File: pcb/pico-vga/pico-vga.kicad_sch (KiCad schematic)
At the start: 32 parts, among them J1 DB15_Female_HighDensity, J2 Micro_SD_Card, J3 AudioJack3, J8 Conn_01x05_Male, J9 Conn_01x02_Male, SW1 SW_Push, U1 Raspberry_Pi_Pico, U2 74LVC2G34

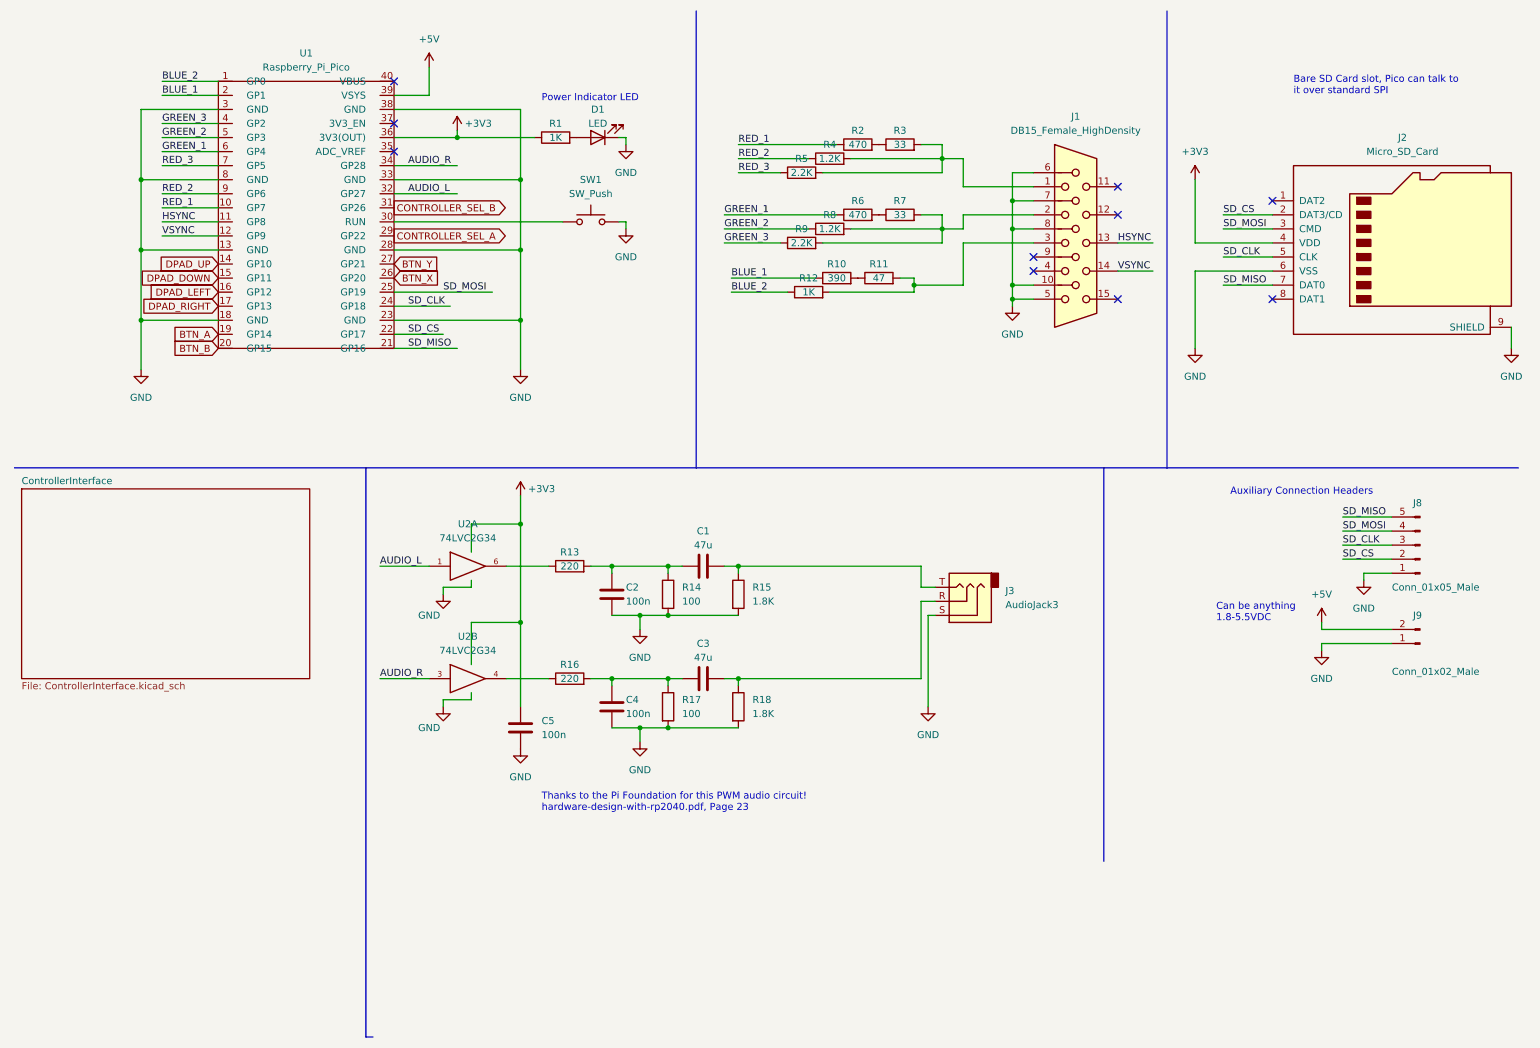
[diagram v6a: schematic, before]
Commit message: PCB v2 done
This update removed most of the stuff on the board -- the massive controller multiplexer is now replaced with an ATTiny24 on the controller side and an I2C bus. The buffer for the audio circuit is also gone. The board now supports surface mounting the pico, and is significantly smaller.
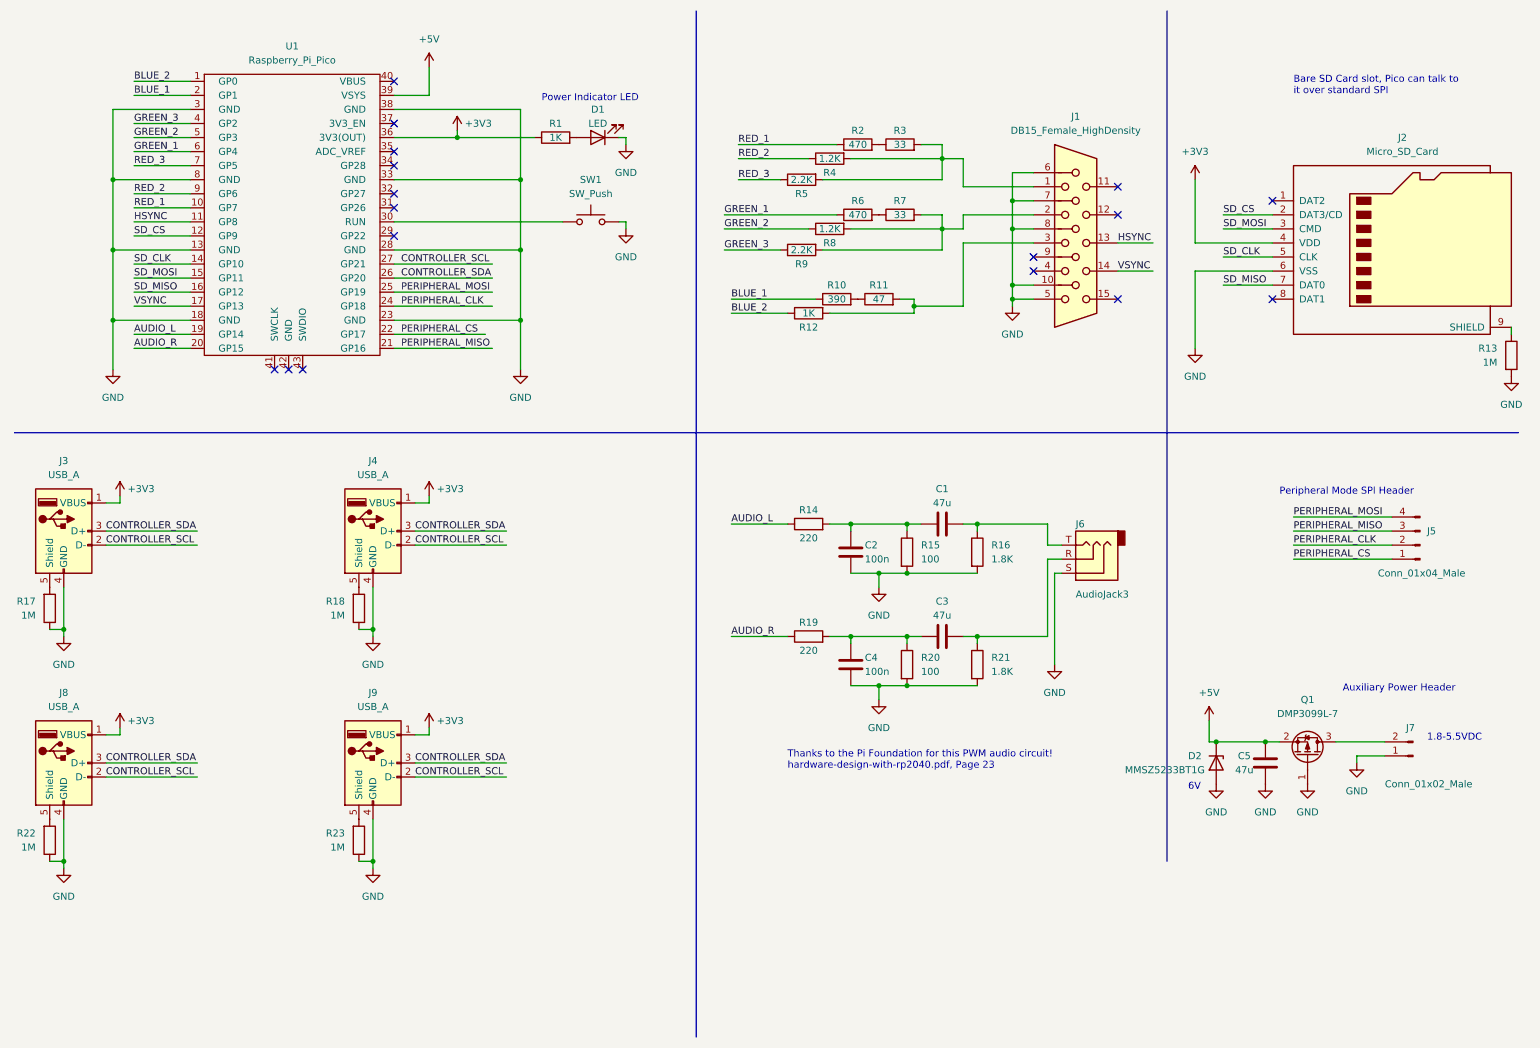
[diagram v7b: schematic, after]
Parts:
- removed J8: Conn_01x05_Male, Connector_PinHeader_2.54mm:PinHeader_1x05_P2.54mm_Horizontal, symbol Connector:Conn_01x05_Male
- removed U2: 74LVC2G34, Package_SO:TSOP-6_1.65x3.05mm_P0.95mm, symbol 74xGxx:74LVC2G34
- added D2: MMSZ5233BT1G, Diode_SMD:D_SOD-123, symbol Device:D_Zener
- added J3, J4, J8, J9: USB_A, Connector_USB:USB_A_Molex_67643_Horizontal, symbol Connector:USB_A
- added J5: Conn_01x04_Male, Connector_PinHeader_2.54mm:PinHeader_1x04_P2.54mm_Horizontal, symbol Connector:Conn_01x04_Male
- added Q1: DMP3099L-7, Package_TO_SOT_SMD:SOT-23, symbol Device:Q_PMOS_GSD
- added R13, R17, R18, R22, R23: 1M, Resistor_SMD:R_0805_2012Metric_Pad1.20x1.40mm_HandSolder, symbol Device:R
- C1, C2, C3, C4: footprint Capacitor_SMD:C_0603_1608Metric_Pad1.08x0.95mm_HandSolder -> Capacitor_SMD:C_0805_2012Metric_Pad1.18x1.45mm_HandSolder
- C5: value 100n -> 47u; footprint Capacitor_SMD:C_0603_1608Metric_Pad1.08x0.95mm_HandSolder -> Capacitor_SMD:C_0805_2012Metric_Pad1.18x1.45mm_HandSolder
- J1: Part Number (none) -> L77HDE15SD1CH4FVGA
- J2: Part Number (none) -> DM3AT-SF-PEJM5
- J6: renamed from J3; Part Number (none) -> SJ1-3533NG
- R1, R10, R11, R12, R2, R3, R4, R5, R6, R7, R8, R9: footprint Resistor_SMD:R_0603_1608Metric_Pad0.98x0.95mm_HandSolder -> Resistor_SMD:R_0805_2012Metric_Pad1.20x1.40mm_HandSolder
- R14: renamed from R13; footprint Resistor_SMD:R_0603_1608Metric_Pad0.98x0.95mm_HandSolder -> Resistor_SMD:R_0805_2012Metric_Pad1.20x1.40mm_HandSolder
- R15: renamed from R14; footprint Resistor_SMD:R_0603_1608Metric_Pad0.98x0.95mm_HandSolder -> Resistor_SMD:R_0805_2012Metric_Pad1.20x1.40mm_HandSolder
- R16: renamed from R15; footprint Resistor_SMD:R_0603_1608Metric_Pad0.98x0.95mm_HandSolder -> Resistor_SMD:R_0805_2012Metric_Pad1.20x1.40mm_HandSolder
- R19: renamed from R16; footprint Resistor_SMD:R_0603_1608Metric_Pad0.98x0.95mm_HandSolder -> Resistor_SMD:R_0805_2012Metric_Pad1.20x1.40mm_HandSolder
- R20: renamed from R17; footprint Resistor_SMD:R_0603_1608Metric_Pad0.98x0.95mm_HandSolder -> Resistor_SMD:R_0805_2012Metric_Pad1.20x1.40mm_HandSolder
- R21: renamed from R18; footprint Resistor_SMD:R_0603_1608Metric_Pad0.98x0.95mm_HandSolder -> Resistor_SMD:R_0805_2012Metric_Pad1.20x1.40mm_HandSolder
- renumbered J9 to J7
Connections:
- net BTN_A is gone; now on net AUDIO_L: U1.19 (GP14)
- net BTN_B is gone; now on net AUDIO_R: U1.20 (GP15)
- net DPAD_DOWN is gone; now on net SD_MOSI: U1.15 (GP11)
- net DPAD_LEFT is gone; now on net SD_MISO: U1.16 (GP12)
- net DPAD_RIGHT is gone; now on net VSYNC: U1.17 (GP13)
- net DPAD_UP is gone; now on net SD_CLK: U1.14 (GP10)
- net +3V3: now also J3.1 (VBUS), J4.1 (VBUS), J8.1 (VBUS), J9.1 (VBUS); no longer C5.1
- net +5V: now also C5.2, D2.1 (K), Q1.2 (S); no longer J7.2 (Pin_2)
- net AUDIO_L: now also R14.1; no longer U1.32 (GP27)
- net AUDIO_R: now also R19.1; no longer U1.34 (GP28)
- net GND: now also C5.1, D2.2 (A), J3.4 (GND), J4.4 (GND), J8.4 (GND), J9.4 (GND), Q1.1 (G), R13.2, R17.1, R18.1, R22.1, R23.1; no longer C5.2, J2.9 (SHIELD)
- net SD_CLK: no longer U1.24 (GP18)
- net SD_CS: now also U1.12 (GP9); no longer U1.22 (GP17)
- net SD_MISO: no longer U1.21 (GP16)
- net SD_MOSI: no longer U1.25 (GP19)
- net VSYNC: no longer U1.12 (GP9)
- net BTN_X renamed CONTROLLER_SDA
- net CONTROLLER_SDA: now also J3.3 (D+), J4.3 (D+), J8.3 (D+), J9.3 (D+)
- net BTN_Y renamed CONTROLLER_SCL
- net CONTROLLER_SCL: now also J3.2 (D-), J4.2 (D-), J8.2 (D-), J9.2 (D-)
- net CONTROLLER_SEL_A: no longer names the net of U1.29 (GP22)
- net CONTROLLER_SEL_B: no longer names the net of U1.31 (GP26)
- new net: J9.5 (Shield), R23.2
- new net: J4.5 (Shield), R18.2
- new net: J3.5 (Shield), R17.2
- new net: J2.9 (SHIELD), R13.1
- new net: J8.5 (Shield), R22.2
- new net: J7.2 (Pin_2), Q1.3 (D)
- new net PERIPHERAL_CLK: J5.2 (Pin_2), U1.24 (GP18)
- new net PERIPHERAL_CS: J5.1 (Pin_1), U1.22 (GP17)
- new net PERIPHERAL_MISO: J5.3 (Pin_3), U1.21 (GP16)
- new net PERIPHERAL_MOSI: J5.4 (Pin_4), U1.25 (GP19)
- no-connect marks 10 -> 17
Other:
- removed sheet ControllerInterface
- note added: "1.8-5.5VDC"
- note added: "6V"
- note added: "Auxiliary Power Header"
- note added: "Peripheral Mode SPI Header"
- note removed: "Auxiliary Connection Headers"
- note removed: "Can be anything 1.8-5.5VDC"
- moved on the sheet: C1, C2, C3, C4, J6, J7, R10, R11, R12, R14, R15, R16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

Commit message: PCB update and BOM
Remade the BOM so now you can just export to csv and throw it into digikey, makes it a lot easier. In making the BOM I realized some of my old parts were super expensive, so I redid some components
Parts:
- removed J2: Micro_SD_Card, Connector_Card:microSD_HC_Hirose_DM3AT-SF-PEJM5, symbol Connector:Micro_SD_Card
- added J2: Micro_SD_Card_Det, pico-vga:MEM2061-01-188-00-A_GCT, symbol Connector:Micro_SD_Card_Det
- J6: footprint Connector_Audio:Jack_3.5mm_CUI_SJ1-3533NG_Horizontal -> pico-vga:STX-3000_KYC
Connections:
- net +3V3: now also J2.4 (VDD)
- net GND: now also J2.6 (VSS)
- net SD_CLK: now also J2.5 (CLK)
- net SD_CS: now also J2.2 (DAT3/CD)
- net SD_MISO: now also J2.7 (DAT0)
- net SD_MOSI: now also J2.3 (CMD)
- net at R13.1: now also J2.11 (SHIELD)
- no-connect marks 17 -> 19
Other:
- note removed: "Bare SD Card slot, Pico can talk to it over standard SPI"
- moved on the sheet: R13
